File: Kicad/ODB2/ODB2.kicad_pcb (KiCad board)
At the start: 4 copper layers, 83.9 x 76.5 mm, 183 parts, among them J4 RF2-04A-T-00-50-G, J5 RFM_Conn_Coaxial, U1 STM32F412ZGTx, U10 W25Q512JVEIQ, U2 TLV2371DBV, U3 74LV1T87GVH, U5 L76L-M33, U6 ICM-20948, U7 MS580301BA01-00

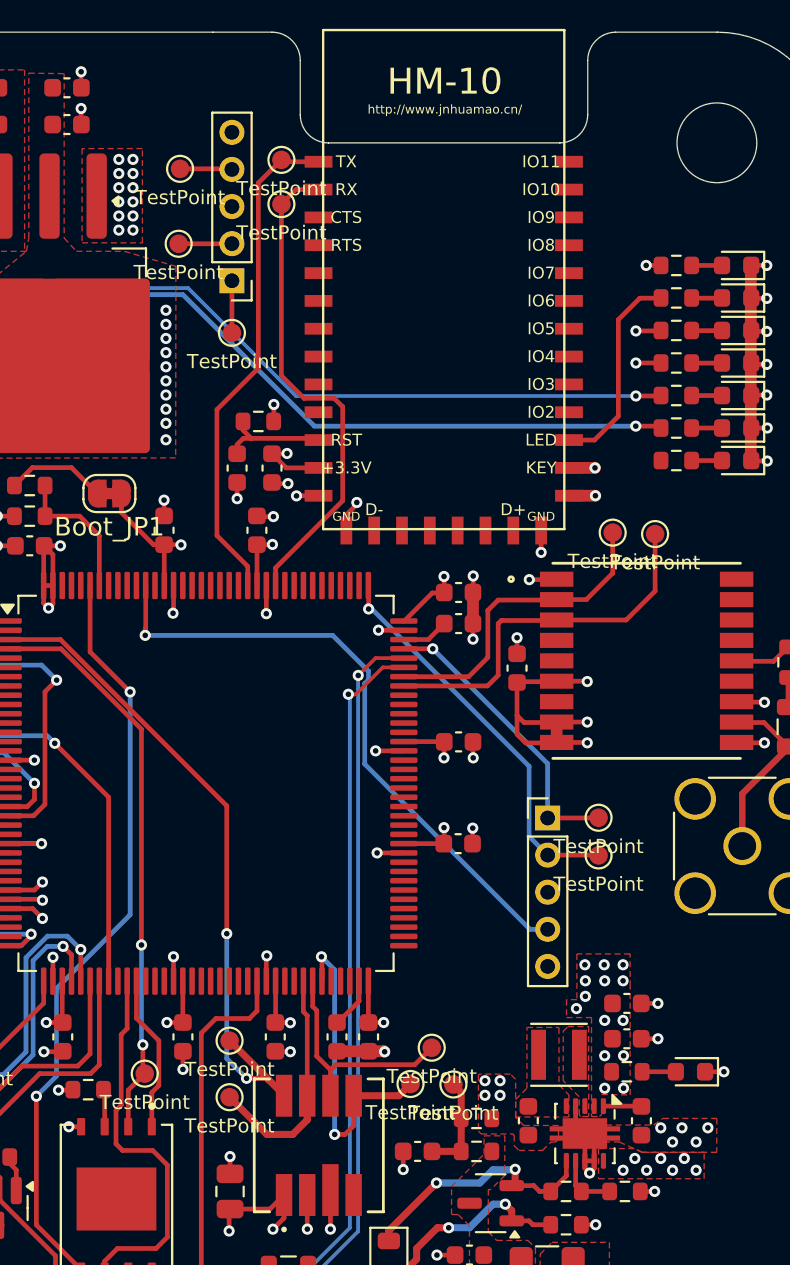
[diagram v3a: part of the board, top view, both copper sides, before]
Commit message: add uart RFD + fix 3v7_An pinout
RFD tx, rx, rts
3v7_An pinout PC2 -> PC5
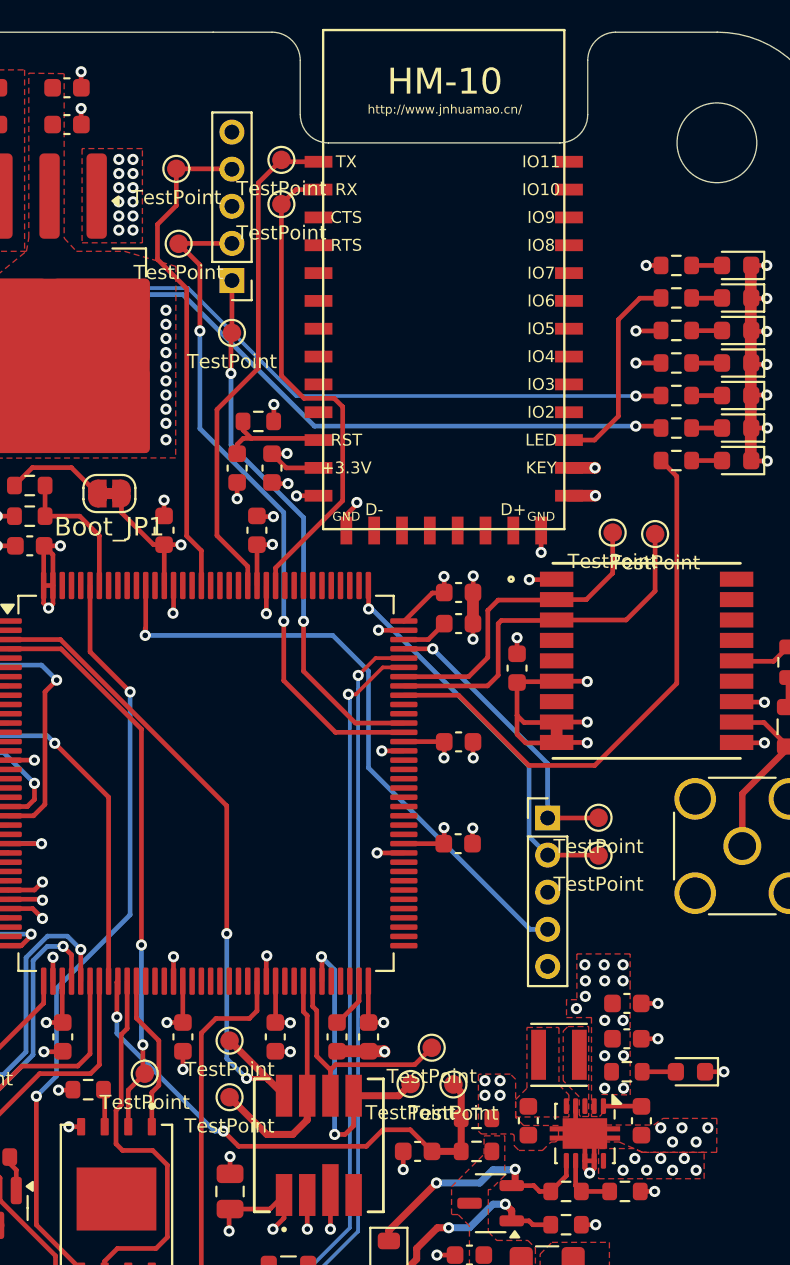
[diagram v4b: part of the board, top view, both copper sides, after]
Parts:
- moved TP18 0.20 mm to (48.8, 7.37)
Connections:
- U1 pad 28: 3v7_An -> unconnected-(U1-PC2-Pad28)
- U1 pad 45: unconnected-(U1-PC5-Pad45) -> 3v7_An
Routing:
- net UART6_RFD_TX: track 2.87 -> 36.4 mm, vias 0 -> 2
- net CriticalLEDEnable: track 0.00 -> 30.5 mm
- net UART6_RFD_RX: track 2.81 -> 29.3 mm, vias 0 -> 2
- net UART6_RFD_RTS: track 2.81 -> 26.9 mm
- net 3v7_An: track 5.36 -> 28.6 mm, vias 0 -> 2

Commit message: fix Pyro_MainADC -> Pyro_ADC
conjoint au drogue et main (selection avec xODB)
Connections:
- net Pyros_MainADC renamed Pyros_ADC
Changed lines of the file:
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@@
 	(net 74 "unconnected-(U1-PC2-Pad28)")
 	(net 75 "Net-(Batt7v4_D2-A)")
-	(net 76 "Pyros_MainADC")
+	(net 76 "Pyros_ADC")
 	(net 77 "unconnected-(Pyros_AND1-4A-Pad12)")
 	(net 78 "Pyros_MainOn")
@@
 			(layers "F.Cu" "F.Paste" "F.Mask")
 			(roundrect_rratio 0.25)
-			(net 76 "Pyros_MainADC")
+			(net 76 "Pyros_ADC")
 			(pinfunction "PC4")
 			(pintype "bidirectional")
@@
 			(layers "F.Cu" "F.Paste" "F.Mask")
 			(roundrect_rratio 0.25)
-			(net 76 "Pyros_MainADC")
+			(net 76 "Pyros_ADC")
 			(pintype "output")
 		)
@@
 			(size 1 1)
 			(layers "F.Cu" "F.Mask")
-			(net 76 "Pyros_MainADC")
+			(net 76 "Pyros_ADC")
 			(pinfunction "1")
 			(pintype "passive")
@@
 			(layers "F.Cu" "F.Paste" "F.Mask")
 			(roundrect_rratio 0.25)
-			(net 76 "Pyros_MainADC")
+			(net 76 "Pyros_ADC")
 			(pintype "passive")
 		)

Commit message: fix + cleanup
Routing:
- net 7v4Enable: track 46.2 -> 44.9 mm, vias 4 -> 3
- net Pyros_Bluetooth: track 25.4 -> 24.2 mm, vias 1 -> 0
- net Net-(E1-LED): vias 0 -> 2
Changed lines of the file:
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@@
 	)
 	(segment
-		(start 71.384 23.485)
-		(end 71.3686 23.4696)
-		(width 0.635)
-		(layer "F.Cu")
-		(net 1)
-	)
-	(segment
 		(start 18.5022 54.88)
 		(end 21.587 54.88)
@@
 	(segment
 		(start 9.0932 11.2268)
-		(end 10.414 9.906)
+		(end 11.938 8.382)
 		(width 0.254)
 		(layer "F.Cu")
@@
 	)
 	(segment
-		(start 10.414 9.906)
-		(end 11.938 8.382)
-		(width 0.254)
-		(layer "F.Cu")
-		(net 15)
-	)
-	(segment
 		(start 16.637 44.132)
 		(end 16.0904 44.6786)
@@
 	)
 	(segment
-		(start 73.58985 16.1036)
-		(end 74.84775 16.1036)
-		(width 0.254)
-		(layer "F.Cu")
-		(net 23)
-	)
-	(segment
 		(start 38.270001 35.237599)
 		(end 38.0492 35.4584)
@@
 	)
 	(via
-		(at 73.58985 16.1036)
-		(size 0.6)
-		(drill 0.3)
-		(layers "F.Cu" "B.Cu")
-		(net 23)
-	)
-	(via
 		(at 38.0492 35.4584)
 		(size 0.6)
@@
 	)
 	(segment
-		(start 73.801 14.337)
-		(end 72.644 15.494)
-		(width 0.254)
+		(start 73.7616 14.3256)
+		(end 74.9432 14.3256)
+		(width 0.2)
 		(layer "F.Cu")
 		(net 31)
 	)
 	(segment
-		(start 72.644 15.494)
-		(end 72.644 20.701)
-		(width 0.254)
+		(start 72.644 20.701)
+		(end 72.644 18.8976)
+		(width 0.2)
 		(layer "F.Cu")
 		(net 31)
 	)
 	(segment
-		(start 74.9433 14.337)
-		(end 73.801 14.337)
+		(start 71.36 21.985)
+		(end 69.9826 21.985)
 		(width 0.254)
 		(layer "F.Cu")
 		(net 31)
 	)
+	(via
+		(at 73.7616 14.3256)
+		(size 0.6)
+		(drill 0.3)
+		(layers "F.Cu" "B.Cu")
+		(net 31)
+	)
+	(via
+		(at 72.644 18.8976)
+		(size 0.6)
+		(drill 0.3)
+		(layers "F.Cu" "B.Cu")
+		(net 31)
+	)
 	(segment
-		(start 71.36 21.985)
-		(end 69.9826 21.985)
-		(width 0.254)
-		(layer "F.Cu")
+		(start 72.644 15.4432)
+		(end 73.7616 14.3256)
+		(width 0.2)
+		(layer "B.Cu")
+		(net 31)
+	)
+	(segment
+		(start 72.644 18.8976)
+		(end 72.644 15.4432)
+		(width 0.2)
+		(layer "B.Cu")
 		(net 31)
 	)
@@
 	)
 	(segment
-		(start 40.193 62.4355)
-		(end 40.1828 62.4253)
-		(width 0.254)
-		(layer "F.Cu")
-		(net 34)
-	)
-	(segment
 		(start 38.1894 60.6298)
 		(end 39.3192 61.7596)
@@
 	)
 	(segment
-		(start 73.58985 17.8308)
-		(end 74.84775 17.8308)
-		(width 0.254)
-		(layer "F.Cu")
-		(net 80)
-	)
-	(segment
 		(start 36.9788 37.0804)
 		(end 37.636 37.7376)
@@
 		(net 80)
 	)
-	(via
-		(at 73.58985 17.8308)
-		(size 0.6)
-		(drill 0.3)
-		(layers "F.Cu" "B.Cu")
-		(net 80)
-	)
 	(segment
 		(start 36.003 30.988)
@@
 	)
 	(segment
-		(start 48.8188 7.366)
-		(end 48.8188 9.3472)
+		(start 47.8028 11.7856)
+		(end 49.3776 13.3604)
 		(width 0.254)
 		(layer "F.Cu")
@@
 	)
 	(segment
-		(start 47.8028 12.2428)
-		(end 49.3776 13.8176)
+		(start 48.8188 7.366)
+		(end 48.8188 9.3472)
 		(width 0.254)
 		(layer "F.Cu")
@@
 	)
 	(segment
-		(start 48.8188 7.366)
-		(end 51.7962 7.366)
+		(start 48.8188 9.3472)
+		(end 47.8028 10.3632)
 		(width 0.254)
 		(layer "F.Cu")
@@
 	(segment
 		(start 47.8028 10.3632)
-		(end 47.8028 12.2428)
+		(end 47.8028 11.7856)
 		(width 0.254)
 		(layer "F.Cu")
@@
 	)
 	(segment
-		(start 48.8188 9.3472)
-		(end 47.8028 10.3632)
+		(start 48.8188 7.366)
+		(end 51.7962 7.366)
 		(width 0.254)
 		(layer "F.Cu")
@@
 	)
 	(segment
-		(start 49.3776 13.8176)
-		(end 49.3776 27.156525)
+		(start 50.169 27.947925)
+		(end 50.169 29.8251)
 		(width 0.254)
 		(layer "F.Cu")
@@
 	)
 	(segment
-		(start 50.169 27.947925)
-		(end 50.169 29.8251)
+		(start 49.3776 13.3604)
+		(end 49.3776 27.156525)
 		(width 0.254)
 		(layer "F.Cu")
@@
 	)
 	(segment
-		(start 50.0888 12.5476)
-		(end 48.9458 11.4046)
-		(width 0.254)
-		(layer "F.Cu")
-		(net 104)
-	)
-	(segment
-		(start 51.8094 11.4046)
-		(end 51.816 11.398)
+		(start 57.3972 37.7376)
+		(end 54.61 34.9504)
 		(width 0.254)
 		(layer "F.Cu")
@@
 	)
 	(segment
-		(start 57.3972 37.7376)
-		(end 54.61 34.9504)
+		(start 50.0888 17.526)
+		(end 50.0888 12.5476)
 		(width 0.254)
 		(layer "F.Cu")
@@
 	)
 	(segment
-		(start 50.0888 16.1036)
-		(end 50.0888 12.5476)
+		(start 50.0888 12.5476)
+		(end 48.9458 11.4046)
 		(width 0.254)
 		(layer "F.Cu")
@@
 	)
 	(via
-		(at 50.0888 16.1036)
+		(at 50.0888 17.526)
 		(size 0.6)
 		(drill 0.3)
@@
 	)
 	(segment
-		(start 50.0888 21.365325)
-		(end 50.0888 16.1036)
+		(start 54.61 25.886525)
+		(end 54.61 31.75)
 		(width 0.254)
 		(layer "B.Cu")
@@
 	)
 	(segment
-		(start 54.61 25.886525)
-		(end 50.0888 21.365325)
+		(start 50.0888 21.365325)
+		(end 54.61 25.886525)
 		(width 0.254)
 		(layer "B.Cu")
@@
 	)
 	(segment
-		(start 54.61 31.75)
-		(end 54.61 25.886525)
+		(start 50.0888 17.526)
+		(end 50.0888 21.365325)
 		(width 0.254)
 		(layer "B.Cu")
@@
 		(width 0.254)
 		(layer "F.Cu")
-		(net 119)
-	)
-	(segment
-		(start 25.6794 54.8132)
-		(end 25.6794 54.5084)
-		(width 0.254)
-		(layer "F.Cu")

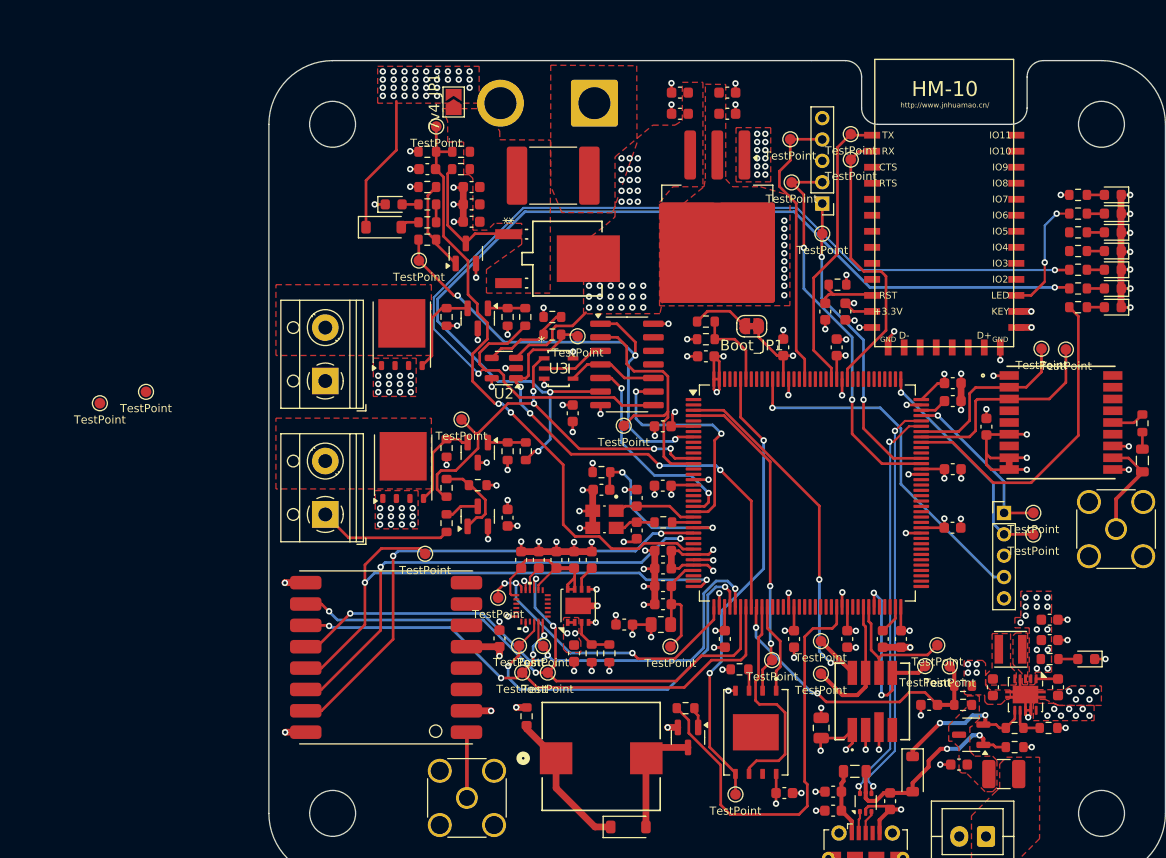
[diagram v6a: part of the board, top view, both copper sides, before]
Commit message: cleanup pcb + set tests pads
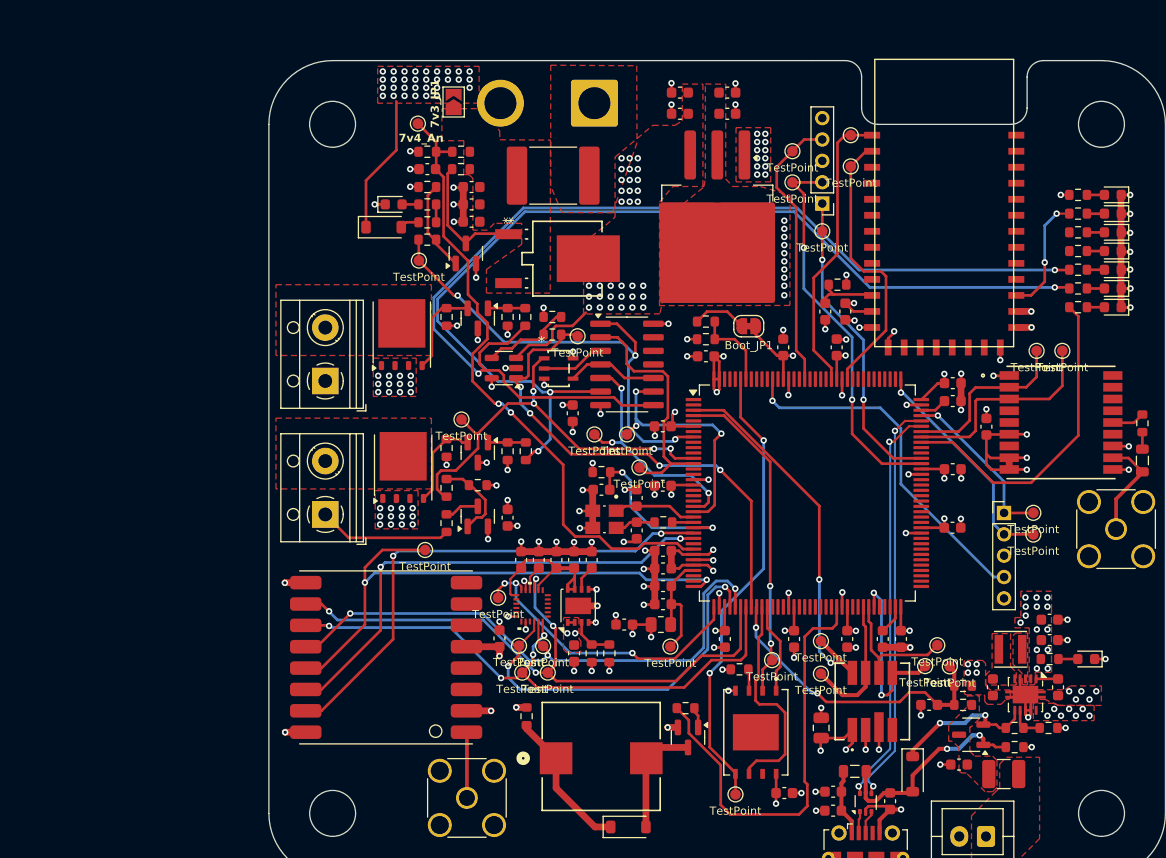
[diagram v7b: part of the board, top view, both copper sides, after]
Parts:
- moved TP24 49.4 mm to (33.5, 35.0)
- moved TP25 42.2 mm to (30.5, 35.0)
- moved TP23 4.18 mm to (34.7, 38.1)
- moved TP14 1.74 mm to (13.9, 5.90)
- moved TP18 1.14 mm to (49.0, 8.48)
- moved TP29 0.63 mm to (54.5, 9.91)
- moved TP8 0.50 mm to (71.9, 27.2)
- moved TP12 0.36 mm to (14.6, 45.8)
- moved TP7 0.35 mm to (74.3, 27.2)
- moved Boot_JP1 0.28 mm to (44.9, 24.9)
- moved TP28 0.23 mm to (51.8, 16.0)
- moved TP31 0.10 mm to (54.5, 6.99)
- moved TP17 0.08 mm to (49.0, 11.4)
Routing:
- net Pyros_MainODB: track 20.0 -> 22.9 mm, vias 2 -> 3
- net Pyros_DrogueODB: track 21.9 -> 23.8 mm, vias 2 -> 3
- net Pyros_Bluetooth: track 24.2 -> 23.0 mm
- net 7v4_An: track 58.9 -> 59.9 mm
- net UART6_RFD_RTS: track 26.9 -> 26.3 mm
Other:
- board text added: "7v3_JP1"
- board text added: "7v4_An"
